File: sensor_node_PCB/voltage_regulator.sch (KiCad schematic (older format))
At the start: 8 parts, among them U1 LD1117S50TR

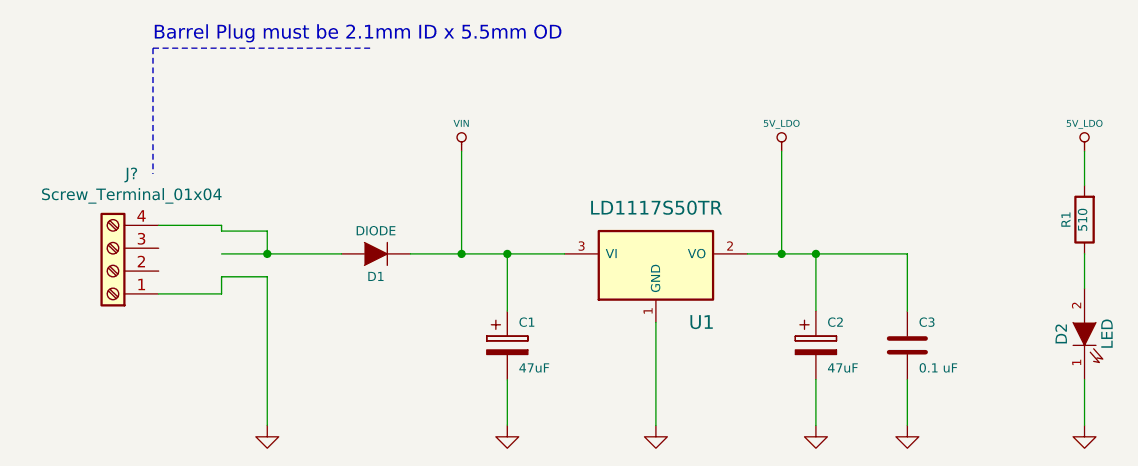
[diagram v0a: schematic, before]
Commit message: changed 12v input to global label
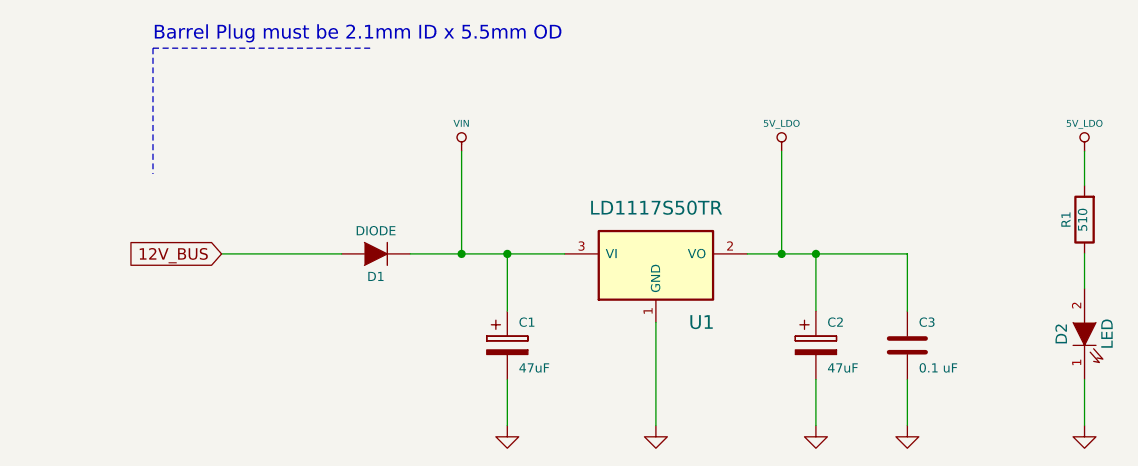
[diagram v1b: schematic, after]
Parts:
- removed J?: Screw_Terminal_01x04, symbol Connector:Screw_Terminal_01x04
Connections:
- net labels added: 12V_BUS
- wire segments 28 -> 19
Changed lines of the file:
@@
 $EndComp
 Wire Wire Line
-	4025 3675 4225 3675
-Wire Wire Line
-	4225 3675 4225 3775
-Connection ~ 4225 3775
-Wire Wire Line
 	5275 3775 5275 4025
-Wire Wire Line
-	4025 3875 4225 3875
-Wire Wire Line
-	4225 3875 4225 4525
 Wire Wire Line
 	5275 4325 5275 4525
@@
 	1    0    0    -1
 $EndComp
-$Comp
-L Arduino_Uno_R3_From_Scratch-rescue:GND #PWR09
-U 1 1 56209A71
-P 4225 4525
-F 0 "#PWR09" H 4225 4275 50  0001 C CNN
-F 1 "GND" H 4225 4375 50  0001 C CNN
-F 2 "" H 4225 4525 60  0000 C CNN
-F 3 "" H 4225 4525 60  0000 C CNN
-F 4 "ANY" H 4225 4525 60  0001 C CNN "Source"
-F 5 "N" H 4225 4525 60  0001 C CNN "Critical"
-F 6 "~" H 4225 4525 60  0001 C CNN "Notes"
-	1    4225 4525
-	1    0    0    -1
-$EndComp
 Wire Wire Line
 	6325 3775 6475 3775
 Wire Wire Line
 	4850 3775 5075 3775
-Wire Wire Line
-	4025 3775 4225 3775
-$Comp
-L Connector:Screw_Terminal_01x04 J?
-U 1 1 5F4E5A9B
-P 3550 3850
-F 0 "J?" H 3468 3425 50  0000 C CNN
-F 1 "Screw_Terminal_01x04" H 3468 3516 50  0000 C CNN
-F 2 "" H 3550 3850 50  0001 C CNN
-F 3 "~" H 3550 3850 50  0001 C CNN
-	1    3550 3850
-	-1   0    0    1
-$EndComp
-Wire Wire Line
-	3750 3650 4025 3650
-Wire Wire Line
-	4025 3650 4025 3675
-Wire Wire Line
-	4225 3775 4550 3775
 Wire Wire Line
 	5275 3775 5525 3775
@@
 	5075 3775 5275 3775
 Wire Wire Line
-	3750 3950 4025 3950
-Wire Wire Line
-	4025 3950 4025 3875
+	4025 3775 4550 3775
+Text GLabel 4025 3775 0    50   Input ~ 0
+12V_BUS
 $EndSCHEMATC
